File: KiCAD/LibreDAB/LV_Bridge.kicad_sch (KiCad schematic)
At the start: 38 parts, among them J1 TS30050050-040, J2 TS30050050-040, J3 TS30050050-040, J4 TS30050050-040, Q1 SP010N01BGHTO, Q2 SP010N01BGHTO, Q3 SP010N01BGHTO, Q4 SP010N01BGHTO, U3 MCP6486UT-E/LT, U4 MCP6486UT-E/LT

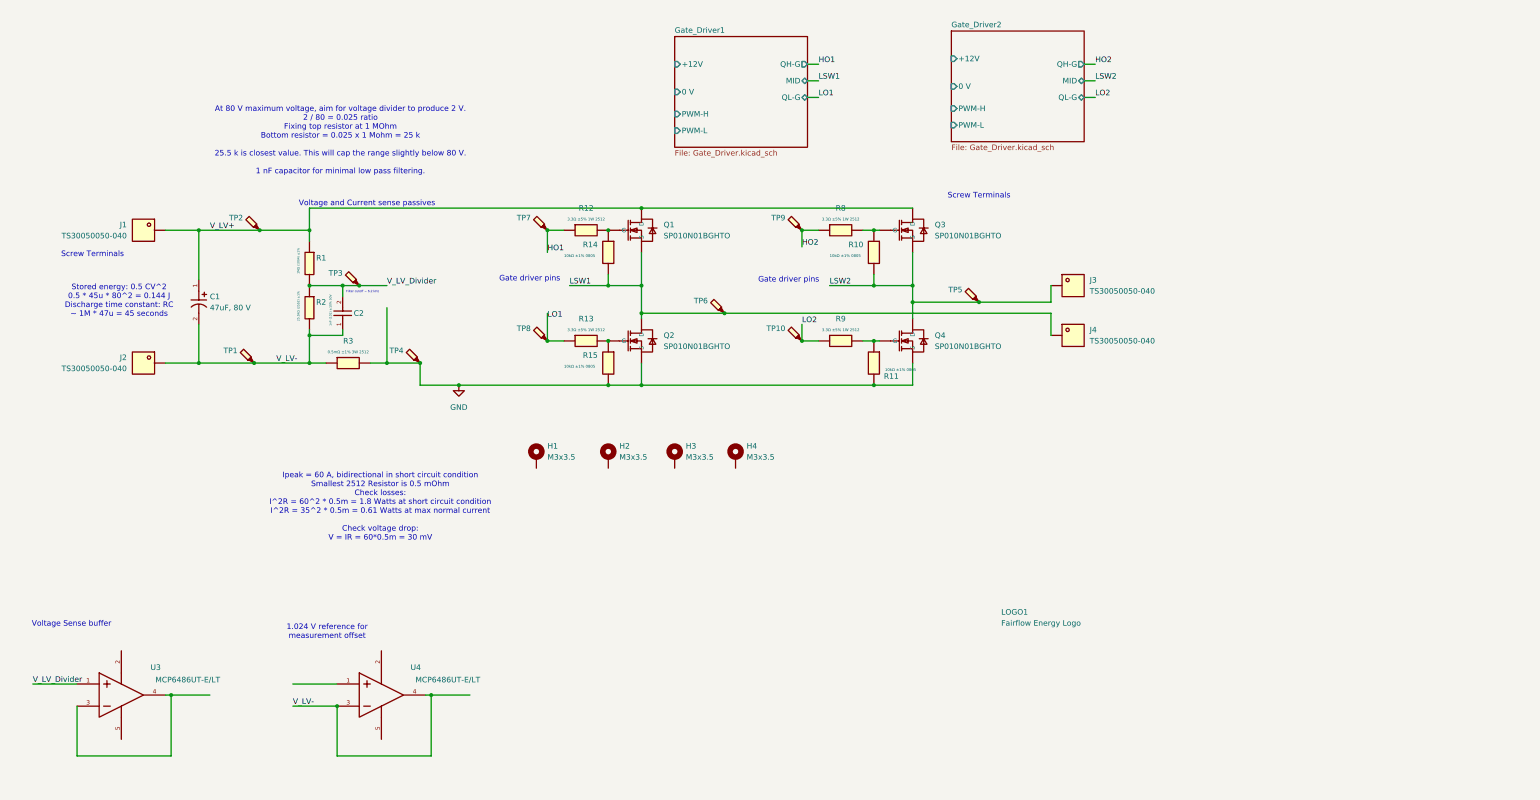
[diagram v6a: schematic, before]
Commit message: Added all major components to LV board
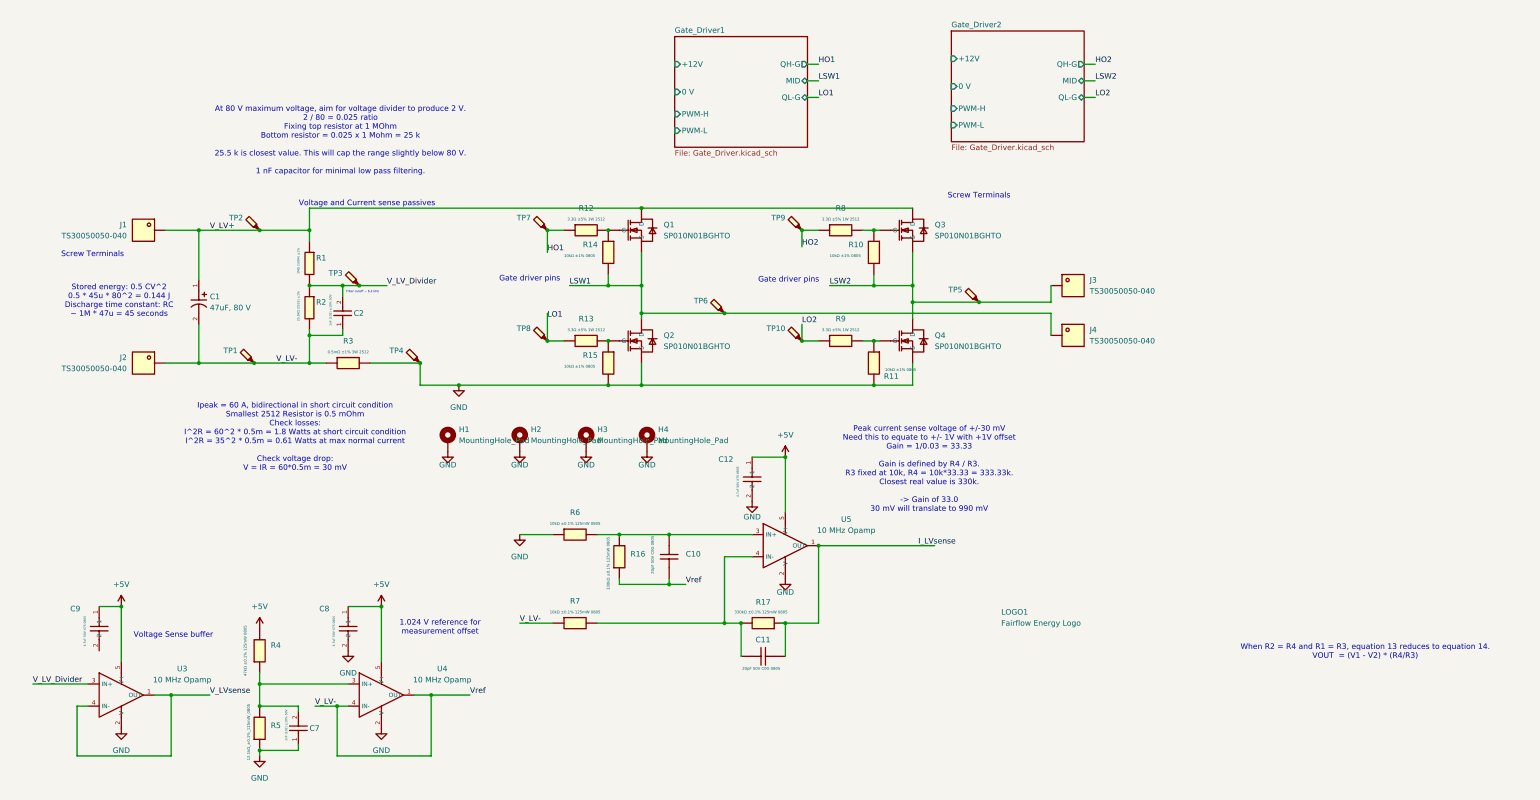
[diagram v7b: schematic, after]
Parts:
- removed U3, U4: MCP6486UT-E/LT, lcsc_footprints:C5224800_SC-70-5_L2_1-W1_3-P0_65-LS2_3-BL, symbol lcsc_imported:MCP6486UT-E/LT
- added C10, C11: 20pF 50V C0G 0805, lcsc_footprints:C176292_C0805, symbol lcsc_imported:20pF 50V C0G 0805
- added C12, C8, C9: 4.7uF 50V X7S 0805, lcsc_footprints:C3861036_C0805, symbol lcsc_imported:GRT21BC71H475KE13L
- added C7: 1nF (102) ±10% 50V, lcsc_footprints:C46653_C0805, symbol lcsc_imported:1nF_(102)_±10%_50V
- added R16, R17: 330kΩ ±0.1% 125mW 0805, lcsc_footprints:C865408_R0805, symbol lcsc_imported:330kΩ ±0.1% 125mW 0805
- added R4: 47kΩ ±0.1% 125mW 0805, lcsc_footprints:C2989281_R0805, symbol lcsc_imported:47kΩ ±0.1% 125mW 0805
- added R5: 12.1kΩ_±0.1%_125mW_0805, lcsc_footprints:C2989281_R0805, symbol lcsc_imported:12.1kΩ_±0.1%_125mW_0805
- added R6, R7: 10kΩ ±0.1% 125mW 0805, lcsc_footprints:C7431042_R0805, symbol lcsc_imported:10kΩ ±0.1% 125mW 0805
- added U3, U4, U5: 10 MHz Opamp, lcsc_footprints:C398358_SOT-23-5_L3_0-W1_7-P0_95-LS2_8-BL, symbol lcsc_imported:TLV9061IDBVR 10 MHz Opamp
- H1, H2, H3, H4: value M3x3.5 -> MountingHole_Pad
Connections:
- net GND: now also H1.1, H2.1, H3.1, H4.1, C12.2, C7.1, C8.2, R5.1, R6.1, U3.2 (V-), U4.2 (V-), U5.2 (V-)
- net V_LV-: now also C10.2, R16.1, R7.1, U4.1 (OUT), U4.4 (IN-)
- net V_LV_Divider: now also U3.3 (IN+)
- new net: C10.1, R16.2, R6.2, U5.3 (IN+)
- new net: C11.1, R17.2, R7.2, U5.4 (IN-)
- new net: C7.2, R4.1, R5.2, U4.3 (IN+)
- new net +5V: C12.1, C8.1, C9.1, R4.2, U3.5 (V+), U4.5 (V+), U5.5 (V+)
- new net I_LVsense: C11.2, R17.1, U5.1 (OUT)
- new net V_LVsense: U3.1 (OUT), U3.4 (IN-)
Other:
- note added: "Peak current sense voltage of +/-30 mV Need this to equate to +/- 1V with +1V offset Gain = 1/0.03 = 33.33 Gain is defined by R4 / R3. R3 fixed at 10k, R4 = 10k*33.33 = 333.33k. Closest real value is 330k. -> Gain of 33.0 30 mV will translate to 990 mV"
- note added: "When R2 = R4 and R1 = R3, equation 13 reduces to equation 14. VOUT = (V1 - V2) * (R4/R3)"
- moved on the sheet: H1, H2, H3, H4

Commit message: LV Stage schematic ready for tidying and layout
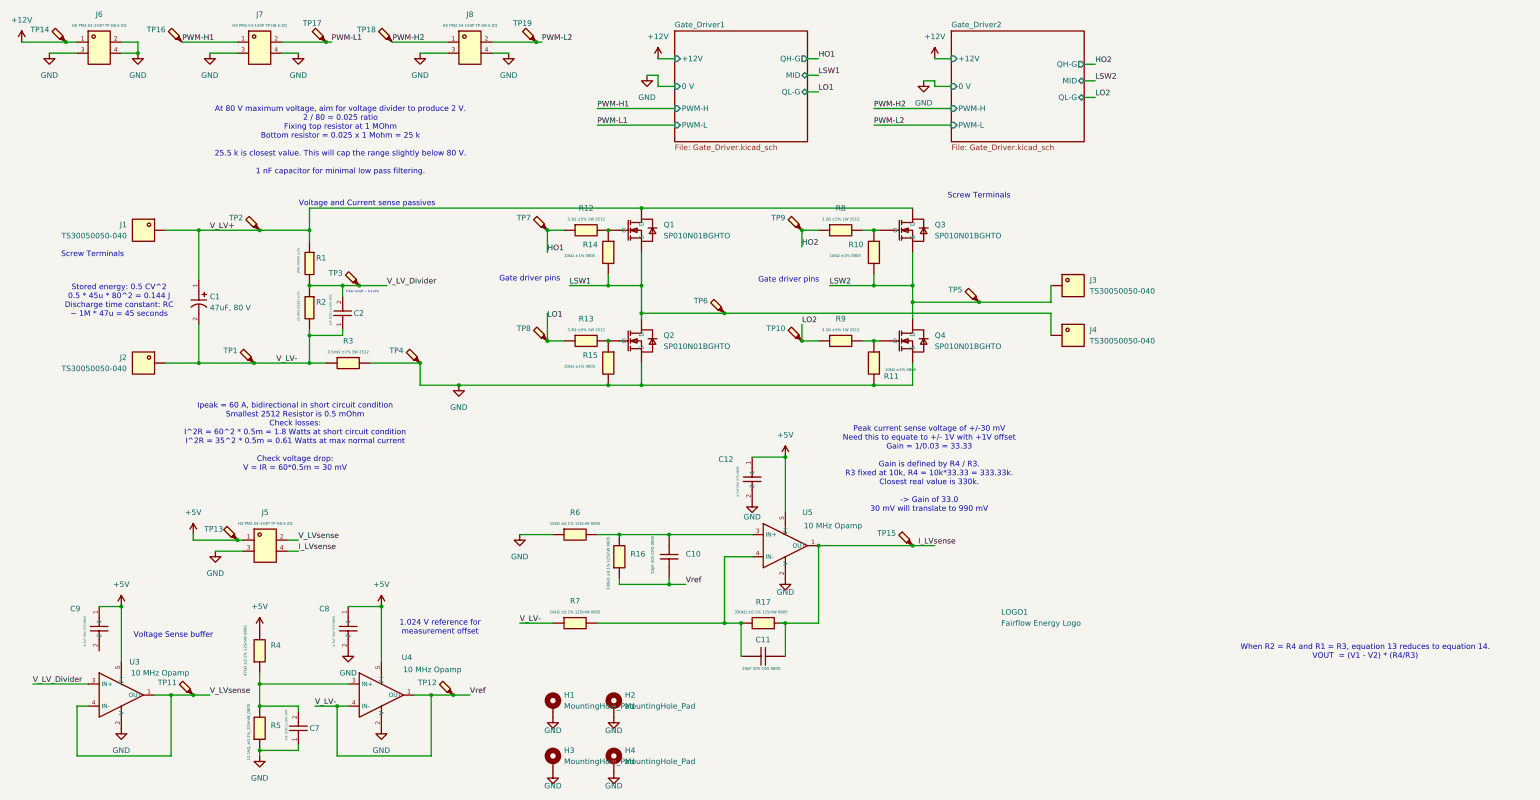
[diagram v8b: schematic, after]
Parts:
- added J5, J6, J7, J8: HX PM2.54-1X4P TP H8.5-ZQ, lcsc_footprints:C48641754_HDR-SMD_4P-P2_54-V-F-LS4_7-R1, symbol lcsc_imported:HX_PM2_54-1X4P_TP_H8_5-ZQ
- added TP11, TP12, TP13, TP14, TP15, TP16, TP17, TP18, TP19: TestPoint_Probe, 1Footprints:TestPoint_Pad_D1.0mm, symbol Connector:TestPoint_Probe
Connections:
- net +5V: now also J5.1, TP13.1
- net GND: now also J5.3, J6.2, J6.3, J6.4, J7.3, J7.4, J8.3, J8.4
- net I_LVsense: now also J5.4, TP15.1
- net V_LV-: now also TP12.1
- net V_LVsense: now also J5.2, TP11.1
- new net +12V: J6.1, TP14.1
- new net PWM-H1: J7.1, TP16.1
- new net PWM-H2: J8.1, TP18.1
- new net PWM-L1: J7.2, TP17.1
- new net PWM-L2: J8.2, TP19.1
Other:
- moved on the sheet: H1, H2, H3, H4
